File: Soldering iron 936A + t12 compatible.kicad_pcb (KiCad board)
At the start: 2 copper layers, 97 x 67 mm, 62 parts, among them J1 DC INPUT, J2 OLED, J3 AC input, J4 output_connector, J5 mosfet_driver_future_backup, Q1 IRF9540N, Q2 BC547, SW1 RotaryEncoder_Switch, U1 LM2596S-ADJ, U2 LM358

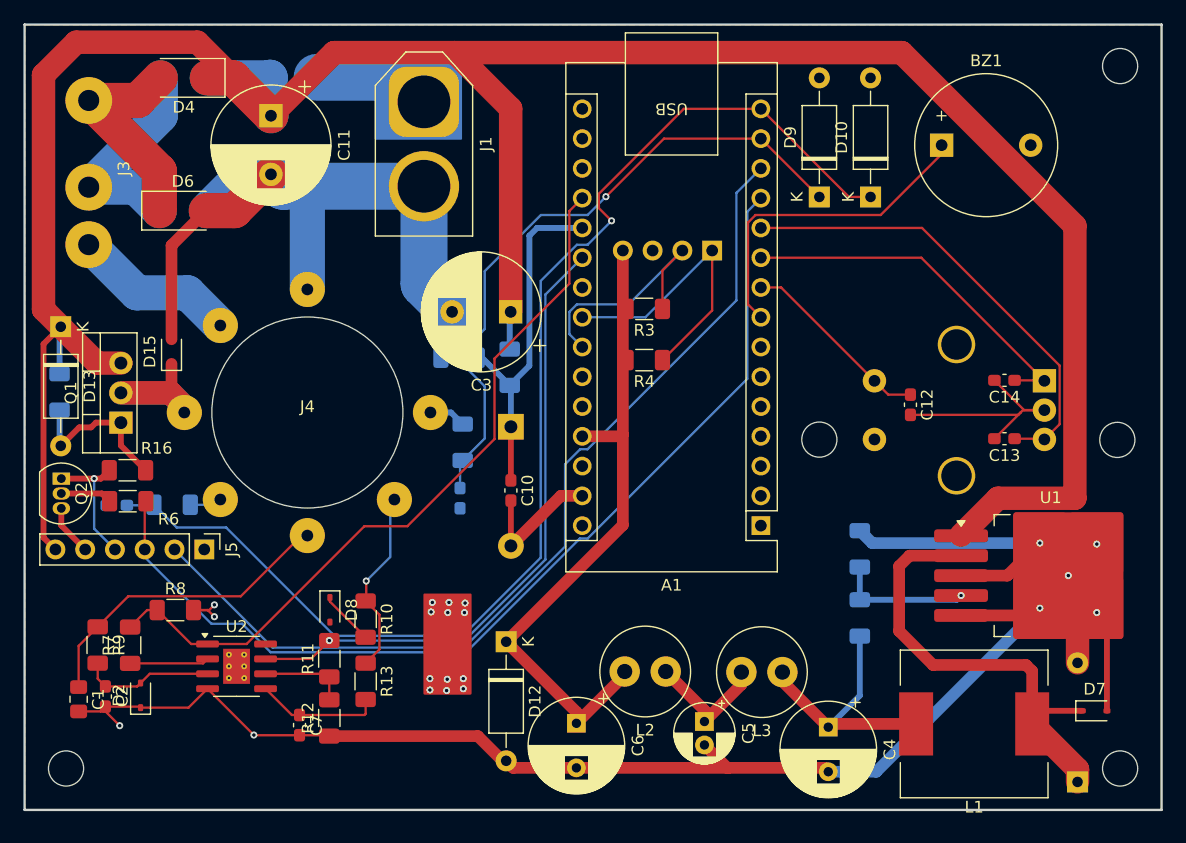
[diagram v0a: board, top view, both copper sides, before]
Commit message: PCB arrived , T12 verified , code updating , Fixed mistakes and redid schmatic
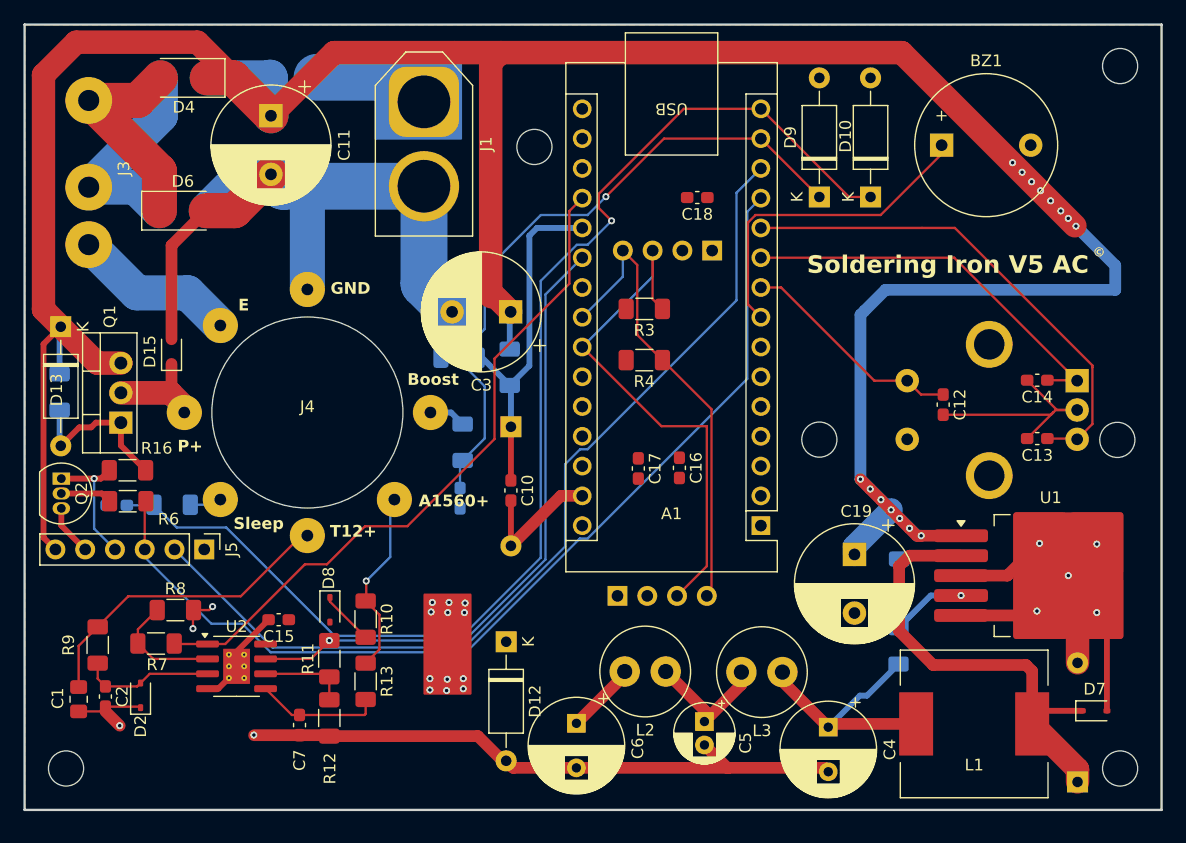
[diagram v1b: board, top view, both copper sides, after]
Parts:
- added C15: 100nf, Capacitor_SMD:C_0603_1608Metric_Pad1.08x0.95mm_HandSolder, F.Cu at (192.6, 116.9)
- added C16: 100nf, Capacitor_SMD:C_0603_1608Metric_Pad1.08x0.95mm_HandSolder, F.Cu at (226.8, 104.0)
- added C17: 100nf, Capacitor_SMD:C_0603_1608Metric_Pad1.08x0.95mm_HandSolder, F.Cu at (223.3, 104.0)
- added C18: 100nf, Capacitor_SMD:C_0603_1608Metric_Pad1.08x0.95mm_HandSolder, F.Cu at (228.3, 80.9)
- added C19: 1000uF, Capacitor_THT:CP_Radial_D10.0mm_P5.00mm, F.Cu at (241.8, 111.4)
- added J6: OLED, Connector_PinHeader_2.54mm:PinHeader_1x04_P2.54mm_Vertical, B.Cu at (221.5, 114.9)
- C5: value 5uF -> 4.7uF
- D1: value ZYxxx -> 5V; footprint Diode_THT:D_DO-41_SOD81_P10.16mm_Horizontal -> Diode_THT:D_A-405_P10.16mm_Horizontal
- D15, D7, D8: value 1N5824 -> 1N5817WS
- D2: value 1N5819WS -> 1N5817WS
- R16: value 6k -> 10k
- R17: value 1k -> 3k
- R2: value 47k -> 100k
- moved R18 4.13 mm to (245.6, 113.3)
- moved R17 4.07 mm to (245.5, 119.2)
- moved C12 2.79 mm to (249.3, 98.6)
- moved C13 2.79 mm to (257.4, 101.5)
- moved C14 2.79 mm to (257.4, 96.5)
- moved SW1 2.79 mm to (260.8, 96.5)
- moved R7 2.22 mm to (182.2, 119.0), turned to 180 degrees
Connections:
- J2 pad 1: /SDA -> +5V
- J2 pad 2: /SCL -> GND
- J2 pad 3: GND -> /SCL
- J2 pad 4: +5V -> /SDA
- R7 pad 1: Net-(U2A--) -> /temp_readback
- R7 pad 2: /temp_readback -> Net-(U2A--)
- R8 pad 1: /temp_readback -> Net-(U2A--)
- U2 pad 9: (no net) -> GND
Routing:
- net +5V: track 56.6 -> 6.13 mm
- net GND: track 241.6 -> 196.7 mm
- net /VIN: track 229.7 -> 268.5 mm, vias 0 -> 15
- net /SCL: track 20.9 -> 45.0 mm
- net /SDA: track 24.5 -> 39.9 mm
- net /temp_readback: track 63.8 -> 58.2 mm
- net Net-(U2A--): track 6.76 -> 10.0 mm
- net /ENCODER S: track 16.5 -> 19.3 mm
- net /ENCODER A: track 31.1 -> 33.9 mm
- net /ENCODER B: track 39.8 -> 42.6 mm
- net Net-(U1-FB): track 11.6 -> 9.26 mm
- net /5v_unfiltered: track 22.8 -> 22.2 mm
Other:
- outline, holes or cut-outs redrawn
- board text added: "A1560+"
- board text added: "Boost"
- board text added: "E"
- board text added: "GND"
- board text added: "P+"
- board text added: "Sleep"
- board text added: "Soldering Iron V5 AC"
- board text added: "T12+"
- board text added: "©"

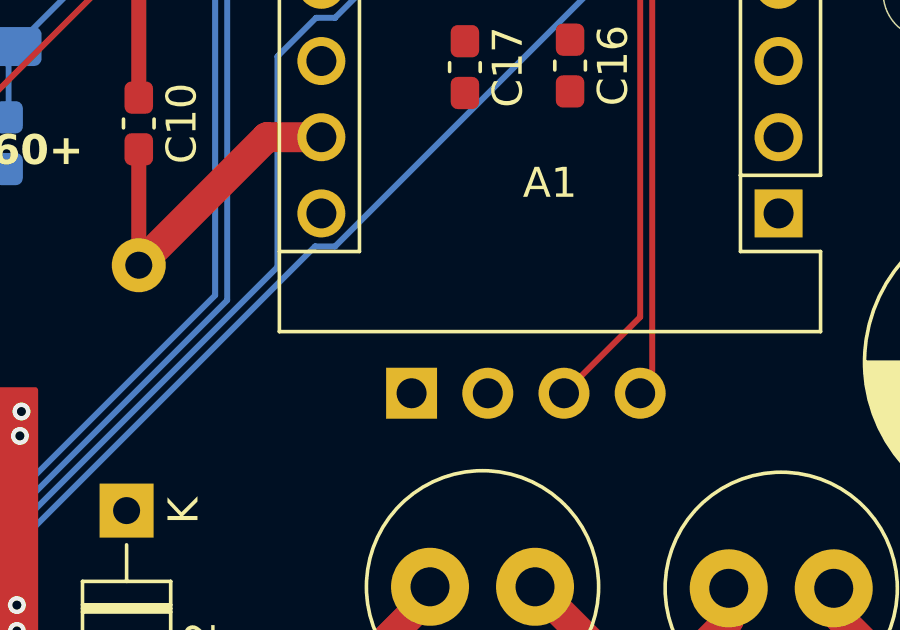
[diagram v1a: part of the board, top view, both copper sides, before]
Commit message: added BOM generation + decoupling Cap for other orination of OLED , Fixed PCB orientation in Readme
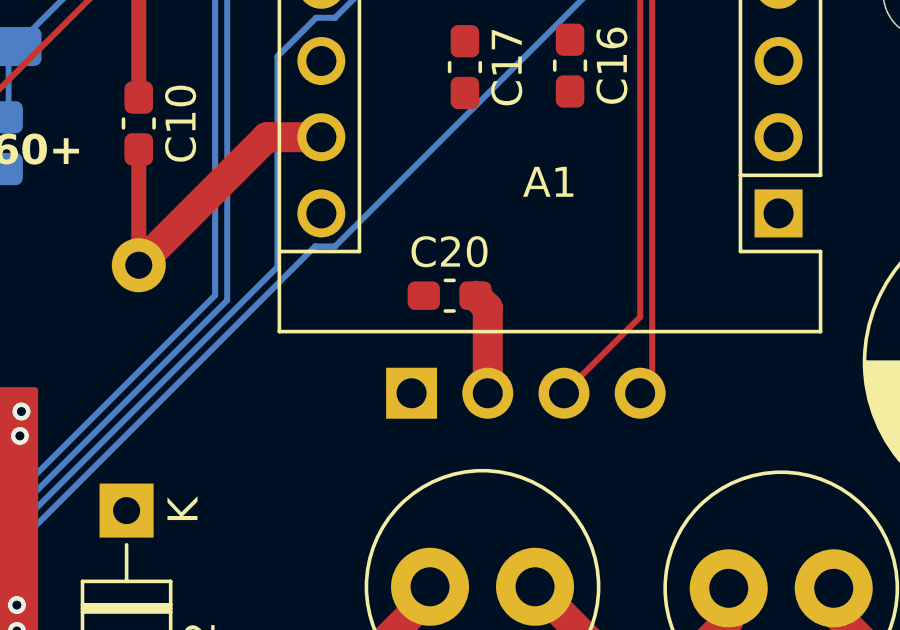
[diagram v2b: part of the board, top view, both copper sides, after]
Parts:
- added C20: 100nf, Capacitor_SMD:C_0603_1608Metric_Pad1.08x0.95mm_HandSolder, F.Cu at (222.8, 111.7)
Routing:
- net GND: track 196.7 -> 200.1 mm
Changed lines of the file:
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@@
 		)
 	)
+	(footprint "Capacitor_SMD:C_0603_1608Metric_Pad1.08x0.95mm_HandSolder"
+		(layer "F.Cu")
+		(at 222.8099 111.6584)
+		(descr "Capacitor SMD 0603 (1608 Metric), square (rectangular) end terminal, IPC_7351 nominal with elongated pad for handsoldering. (Body size source: IPC-SM-782 page 76, https://www.pcb-3d.com/wordpress/wp-content/uploads/ipc-sm-782a_amendment_1_and_2.pdf), generated with kicad-footprint-generator")
+		(tags "capacitor handsolder")
+		(property "Reference" "C20"
+			(at 0 -1.43 0)
+			(layer "F.SilkS")
+			(effects
+				(font
+					(size 1 1)
+					(thickness 0.15)
+				)
+			)
+		)
+		(property "Value" "100nf"
+			(at 0 1.43 0)
+			(layer "F.Fab")
+			(effects
+				(font
+					(size 1 1)
+					(thickness 0.15)
+				)
+			)
+		)
+		(property "Datasheet" ""
+			(at 0 0 0)
+			(unlocked yes)
+			(layer "F.Fab")
+			(hide yes)
+			(effects
+				(font
+					(size 1.27 1.27)
+					(thickness 0.15)
+				)
+			)
+		)
+		(property "Description" "Unpolarized capacitor"
+			(at 0 0 0)
+			(unlocked yes)
+			(layer "F.Fab")
+			(hide yes)
+			(effects
+				(font
+					(size 1.27 1.27)
+					(thickness 0.15)
+				)
+			)
+		)
+		(property ki_fp_filters "C_*")
+		(sheetname "/")
+		(sheetfile "Soldering iron 936A + t12 compatible.kicad_sch")
+		(attr smd)
+		(fp_line
+			(start -0.146267 -0.51)
+			(end 0.146267 -0.51)
+			(stroke
+				(width 0.12)
+				(type solid)
+			)
+			(layer "F.SilkS")
+		)
+		(fp_line
+			(start -0.146267 0.51)
+			(end 0.146267 0.51)
+			(stroke
+				(width 0.12)
+				(type solid)
+			)
+			(layer "F.SilkS")
+		)
+		(fp_line
+			(start -1.65 -0.73)
+			(end 1.65 -0.73)
+			(stroke
+				(width 0.05)
+				(type solid)
+			)
+			(layer "F.CrtYd")
+		)
+		(fp_line
+			(start -1.65 0.73)
+			(end -1.65 -0.73)
+			(stroke
+				(width 0.05)
+				(type solid)
+			)
+			(layer "F.CrtYd")
+		)
+		(fp_line
+			(start 1.65 -0.73)
+			(end 1.65 0.73)
+			(stroke
+				(width 0.05)
+				(type solid)
+			)
+			(layer "F.CrtYd")
+		)
+		(fp_line
+			(start 1.65 0.73)
+			(end -1.65 0.73)
+			(stroke
+				(width 0.05)
+				(type solid)
+			)
+			(layer "F.CrtYd")
+		)
+		(fp_line
+			(start -0.8 -0.4)
+			(end 0.8 -0.4)
+			(stroke
+				(width 0.1)
+				(type solid)
+			)
+			(layer "F.Fab")
+		)
+		(fp_line
+			(start -0.8 0.4)
+			(end -0.8 -0.4)
+			(stroke
+				(width 0.1)
+				(type solid)
+			)
+			(layer "F.Fab")
+		)
+		(fp_line
+			(start 0.8 -0.4)
+			(end 0.8 0.4)
+			(stroke
+				(width 0.1)
+				(type solid)
+			)
+			(layer "F.Fab")
+		)
+		(fp_line
+			(start 0.8 0.4)
+			(end -0.8 0.4)
+			(stroke
+				(width 0.1)
+				(type solid)
+			)
+			(layer "F.Fab")
+		)
+		(fp_text user "${REFERENCE}"
+			(at 0 0 0)
+			(layer "F.Fab")
+			(effects
+				(font
+					(size 0.4 0.4)
+					(thickness 0.06)
+				)
+			)
+		)
+		(pad "1" smd roundrect
+			(at -0.8625 0)
+			(size 1.075 0.95)
+			(layers "F.Cu" "F.Mask" "F.Paste")
+			(roundrect_rratio 0.25)
+			(net 27 "+5V")
+			(pintype "passive")
+		)
+		(pad "2" smd roundrect
+			(at 0.8625 0)
+			(size 1.075 0.95)
+			(layers "F.Cu" "F.Mask" "F.Paste")
+			(roundrect_rratio 0.25)
+			(net 4 "GND")
+			(pintype "passive")
+		)
+		(embedded_fonts no)
+		(model "${KICAD9_3DMODEL_DIR}/Capacitor_SMD.3dshapes/C_0603_1608Metric.wrl"
+			(offset
+				(xyz 0 0 0)
+			)
+			(scale
+				(xyz 1 1 1)
+			)
+			(rotate
+				(xyz 0 0 0)
+			)
+		)
+	)
 	(footprint "Connector_PinHeader_2.54mm:PinHeader_1x04_P2.54mm_Vertical"
 		(layer "B.Cu")
@@
 	)
 	(segment
+		(start 224.0788 114.9096)
+		(end 224.0788 112.0648)
+		(width 1)
+		(layer "F.Cu")
+		(net 4)
+	)
+	(segment
 		(start 263.2964 124.714)
 		(end 263.2964 116.8248)
@@
 		(layer "F.Cu")
 		(net 4)
+	)
+	(segment
+		(start 224.0788 112.0648)
+		(end 223.6724 111.6584)
+		(width 1)
+		(layer "F.Cu")
+		(net 4)

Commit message: Added all 3d models
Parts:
- J1: moved to B.Cu
